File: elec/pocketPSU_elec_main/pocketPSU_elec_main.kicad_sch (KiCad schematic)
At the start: 0 parts

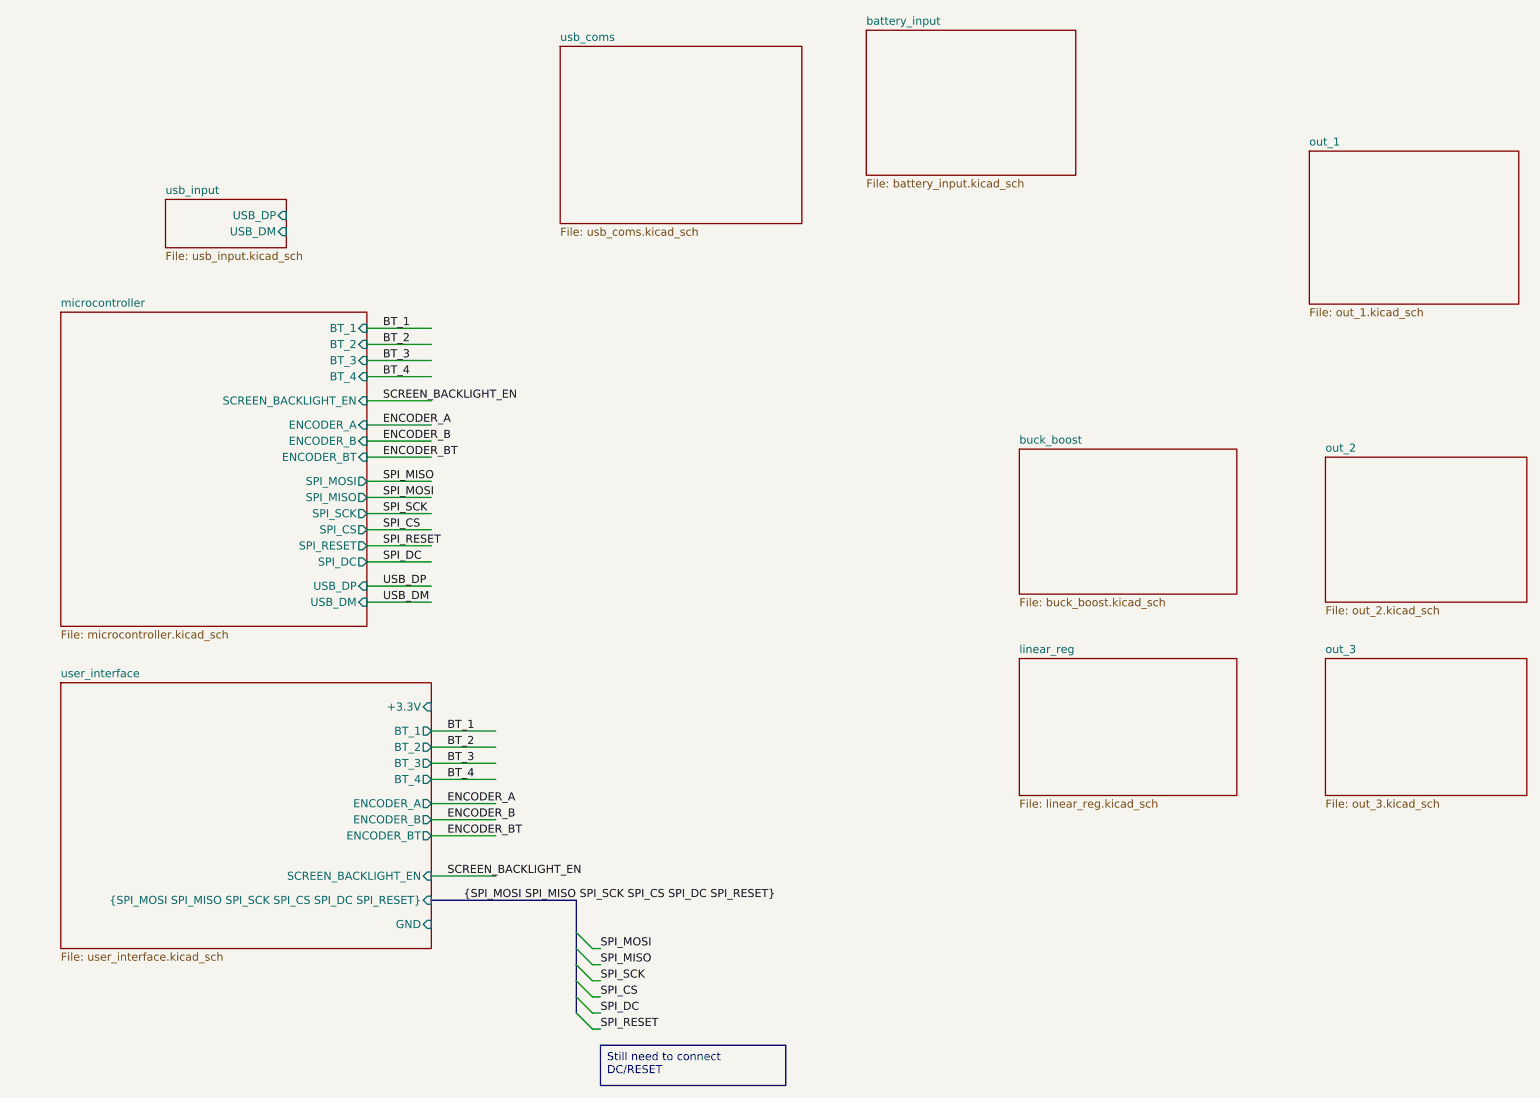
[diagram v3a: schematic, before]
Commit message: add usb coms chip
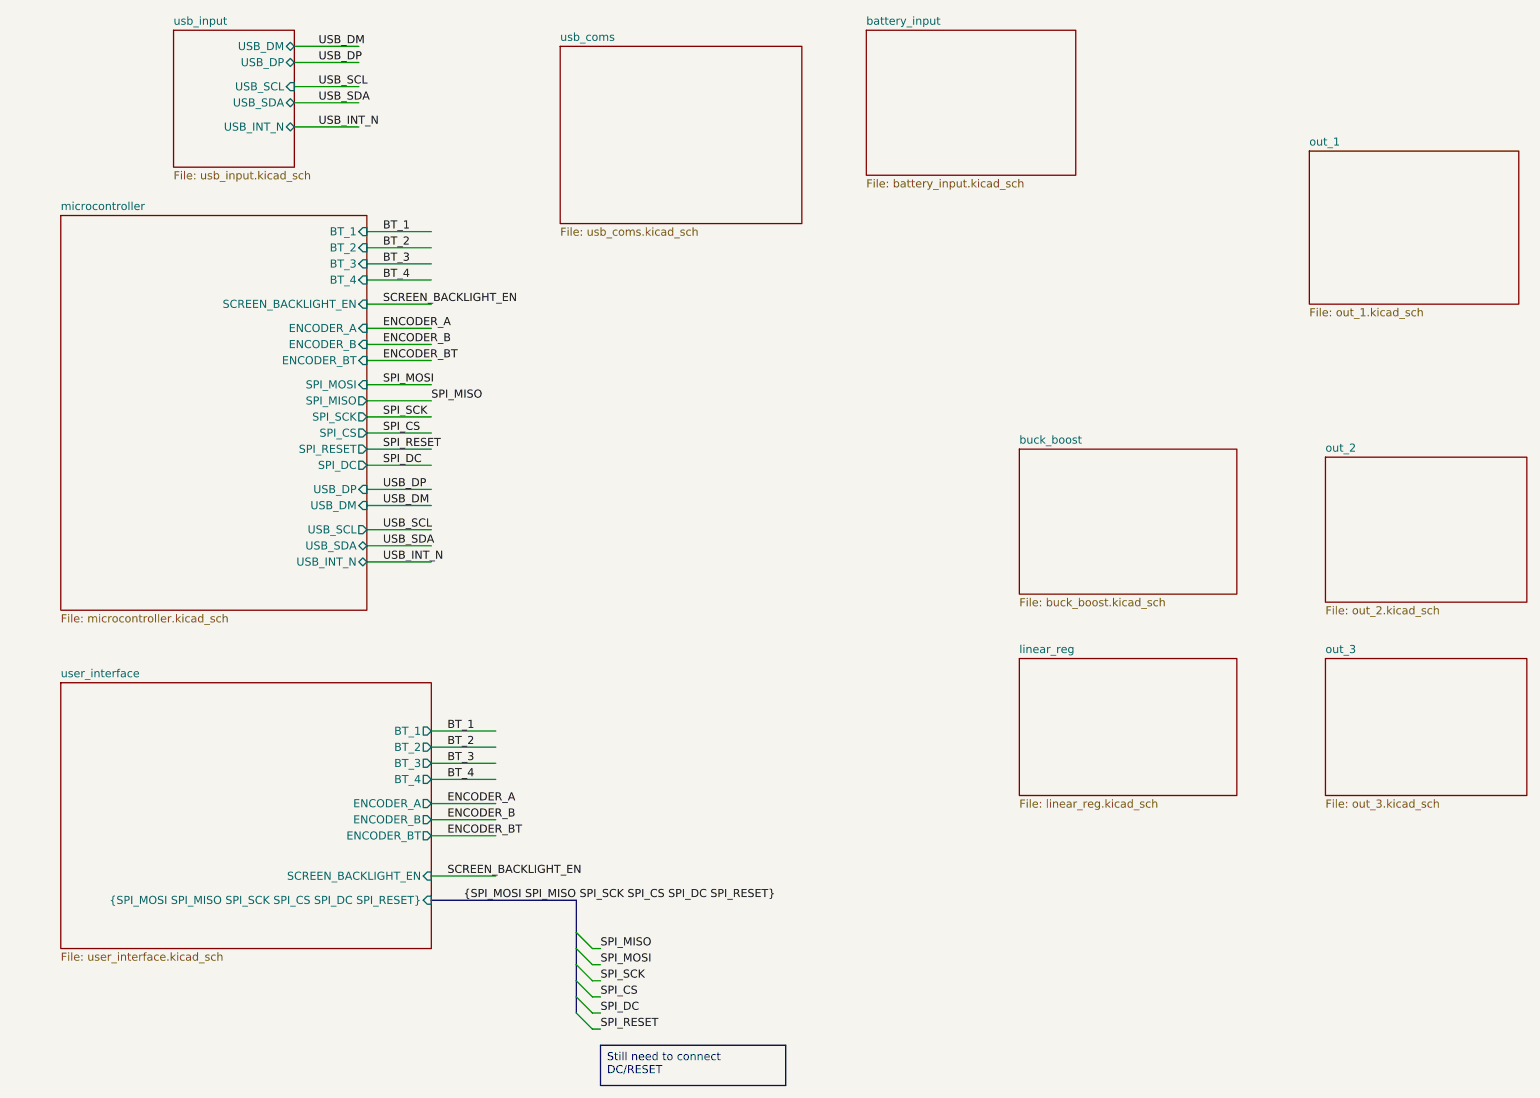
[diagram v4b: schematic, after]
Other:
- sheet microcontroller ports: added USB_INT_N, USB_SCL, USB_SDA; removed none
- sheet usb_input ports: added USB_INT_N, USB_SCL, USB_SDA; removed none
- sheet user_interface ports: added none; removed +3.3V, GND
